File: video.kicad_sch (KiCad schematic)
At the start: 53 parts, among them IC103 HUC6260, IC108 UPC358, J1 RF, Q101 25C945, Q102 25A733, Q103 25C945

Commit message: Work out numbering of and route some caps.
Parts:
- C101: footprint (none) -> A-PCENGINE:Elec_P5.00mm
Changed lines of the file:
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@@
       (effects (font (size 1.27 1.27)))
     )
-    (property "Footprint" "" (at 102.87 93.6752 0)
+    (property "Footprint" "A-PCENGINE:Elec_P5.00mm" (at 102.87 93.6752 0)
       (effects (font (size 1.27 1.27)) hide)
     )
@@
         )
         (path "/c1c718c6-a427-431e-a18b-e46f94ae8e09/c78d7e8a-3e65-46f4-91f4-96eb31925bea"
-          (reference "C141") (unit 1)
+          (reference "C108") (unit 1)
         )
       )
@@
         )
         (path "/c1c718c6-a427-431e-a18b-e46f94ae8e09/c78d7e8a-3e65-46f4-91f4-96eb31925bea"
-          (reference "C112") (unit 1)
+          (reference "CX112") (unit 1)
         )
       )
@@
       (effects (font (size 1.27 1.27)))
     )
-    (property "Footprint" "" (at 102.87 127.9652 0)
+    (property "Footprint" "A-PCENGINE:Elec_P5.00mm" (at 102.87 127.9652 0)
       (effects (font (size 1.27 1.27)) hide)
     )
@@
         )
         (path "/c1c718c6-a427-431e-a18b-e46f94ae8e09/c78d7e8a-3e65-46f4-91f4-96eb31925bea"
-          (reference "C146") (unit 1)
+          (reference "C114") (unit 1)
         )
       )
@@
       (effects (font (size 1.27 1.27)))
     )
-    (property "Footprint" "" (at 91.44 110.1852 0)
+    (property "Footprint" "A-PCENGINE:Elec_P5.00mm" (at 91.44 110.1852 0)
       (effects (font (size 1.27 1.27)) hide)
     )
@@
         )
         (path "/c1c718c6-a427-431e-a18b-e46f94ae8e09/c78d7e8a-3e65-46f4-91f4-96eb31925bea"
-          (reference "C144") (unit 1)
+          (reference "C111") (unit 1)
         )
       )
@@
       (effects (font (size 1.27 1.27)))
     )
-    (property "Footprint" "" (at 91.44 133.0452 0)
+    (property "Footprint" "A-PCENGINE:Elec_P5.00mm" (at 91.44 133.0452 0)
       (effects (font (size 1.27 1.27)) hide)
     )
@@
         )
         (path "/c1c718c6-a427-431e-a18b-e46f94ae8e09/c78d7e8a-3e65-46f4-91f4-96eb31925bea"
-          (reference "C149") (unit 1)
+          (reference "C115") (unit 1)
         )
       )
@@
       (effects (font (size 1.27 1.27)))
     )
-    (property "Footprint" "" (at 102.87 105.1052 0)
+    (property "Footprint" "A-PCENGINE:Elec_P5.00mm" (at 102.87 105.1052 0)
       (effects (font (size 1.27 1.27)) hide)
     )
@@
         )
         (path "/c1c718c6-a427-431e-a18b-e46f94ae8e09/c78d7e8a-3e65-46f4-91f4-96eb31925bea"
-          (reference "C145") (unit 1)
+          (reference "C110") (unit 1)
         )
       )
@@
         )
         (path "/c1c718c6-a427-431e-a18b-e46f94ae8e09/c78d7e8a-3e65-46f4-91f4-96eb31925bea"
-          (reference "C114") (unit 1)
+          (reference "CX114") (unit 1)
         )
       )
@@
       (effects (font (size 1.27 1.27)))
     )
-    (property "Footprint" "" (at 102.87 139.3952 0)
+    (property "Footprint" "A-PCENGINE:Elec_P5.00mm" (at 102.87 139.3952 0)
       (effects (font (size 1.27 1.27)) hide)
     )
@@
         )
         (path "/c1c718c6-a427-431e-a18b-e46f94ae8e09/c78d7e8a-3e65-46f4-91f4-96eb31925bea"
-          (reference "C142") (unit 1)
+          (reference "C116") (unit 1)
         )
       )
@@
       (effects (font (size 1.27 1.27)))
     )
-    (property "Footprint" "" (at 102.87 116.5352 0)
+    (property "Footprint" "A-PCENGINE:Elec_P5.00mm" (at 102.87 116.5352 0)
       (effects (font (size 1.27 1.27)) hide)
     )
@@
         )
         (path "/c1c718c6-a427-431e-a18b-e46f94ae8e09/c78d7e8a-3e65-46f4-91f4-96eb31925bea"
-          (reference "C148") (unit 1)
+          (reference "C112") (unit 1)
         )
       )
@@
       (effects (font (size 1.27 1.27)))
     )
-    (property "Footprint" "" (at 91.44 121.6152 0)
+    (property "Footprint" "A-PCENGINE:Elec_P5.00mm" (at 91.44 121.6152 0)
       (effects (font (size 1.27 1.27)) hide)
     )
@@
         )
         (path "/c1c718c6-a427-431e-a18b-e46f94ae8e09/c78d7e8a-3e65-46f4-91f4-96eb31925bea"
-          (reference "C147") (unit 1)
+          (reference "C113") (unit 1)
         )
       )
@@
       (effects (font (size 1.27 1.27)))
     )
-    (property "Footprint" "" (at 351.4852 101.6 0)
+    (property "Footprint" "A-PCENGINE:Elec_P5.00mm" (at 351.4852 101.6 0)
       (effects (font (size 1.27 1.27)) hide)
     )
@@
       (effects (font (size 1.27 1.27)))
     )
-    (property "Footprint" "" (at 91.44 98.7552 0)
+    (property "Footprint" "A-PCENGINE:Elec_P5.00mm" (at 91.44 98.7552 0)
       (effects (font (size 1.27 1.27)) hide)
     )
@@
         )
         (path "/c1c718c6-a427-431e-a18b-e46f94ae8e09/c78d7e8a-3e65-46f4-91f4-96eb31925bea"
-          (reference "C143") (unit 1)
-        )
-      )
+          (reference "C109") (unit 1)
+        )
+      )

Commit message: Intermediate save
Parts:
- C104, C105, C106, C107: footprint (none) -> A-PCENGINE:SMD_1206_C
- C107, R103, R104: footprint (none) -> A-PCENGINE:SMD_1206
- FL103: footprint (none) -> A-PCENGINE:FL-5.00mm
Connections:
- net +5V: now also IC103.1 (VCC), IC103.13 (VCC), IC103.16 (VCC), IC103.53 (VCC), IC103.54 (VCC), IC103.57 (VCC)
- net +5VA: now also IC103.21 (AVCC), IC103.27 (AVCC), IC103.34 (AVCC), IC103.36 (AVCC), IC103.41 (AVCC), IC103.50 (AVCC)
- net GND: now also IC103.14 (GND), IC103.15 (GND), IC103.3 (GND), IC103.55 (GND), IC103.56 (GND); no longer R103.2
- net GNDA: now also IC103.19 (AGND), IC103.25 (AGND), IC103.29 (AGND), IC103.32 (AGND), IC103.39 (AGND), IC103.48 (AGND)
- new net OSC_GND: R103.2
- no-connect marks 1 -> 4

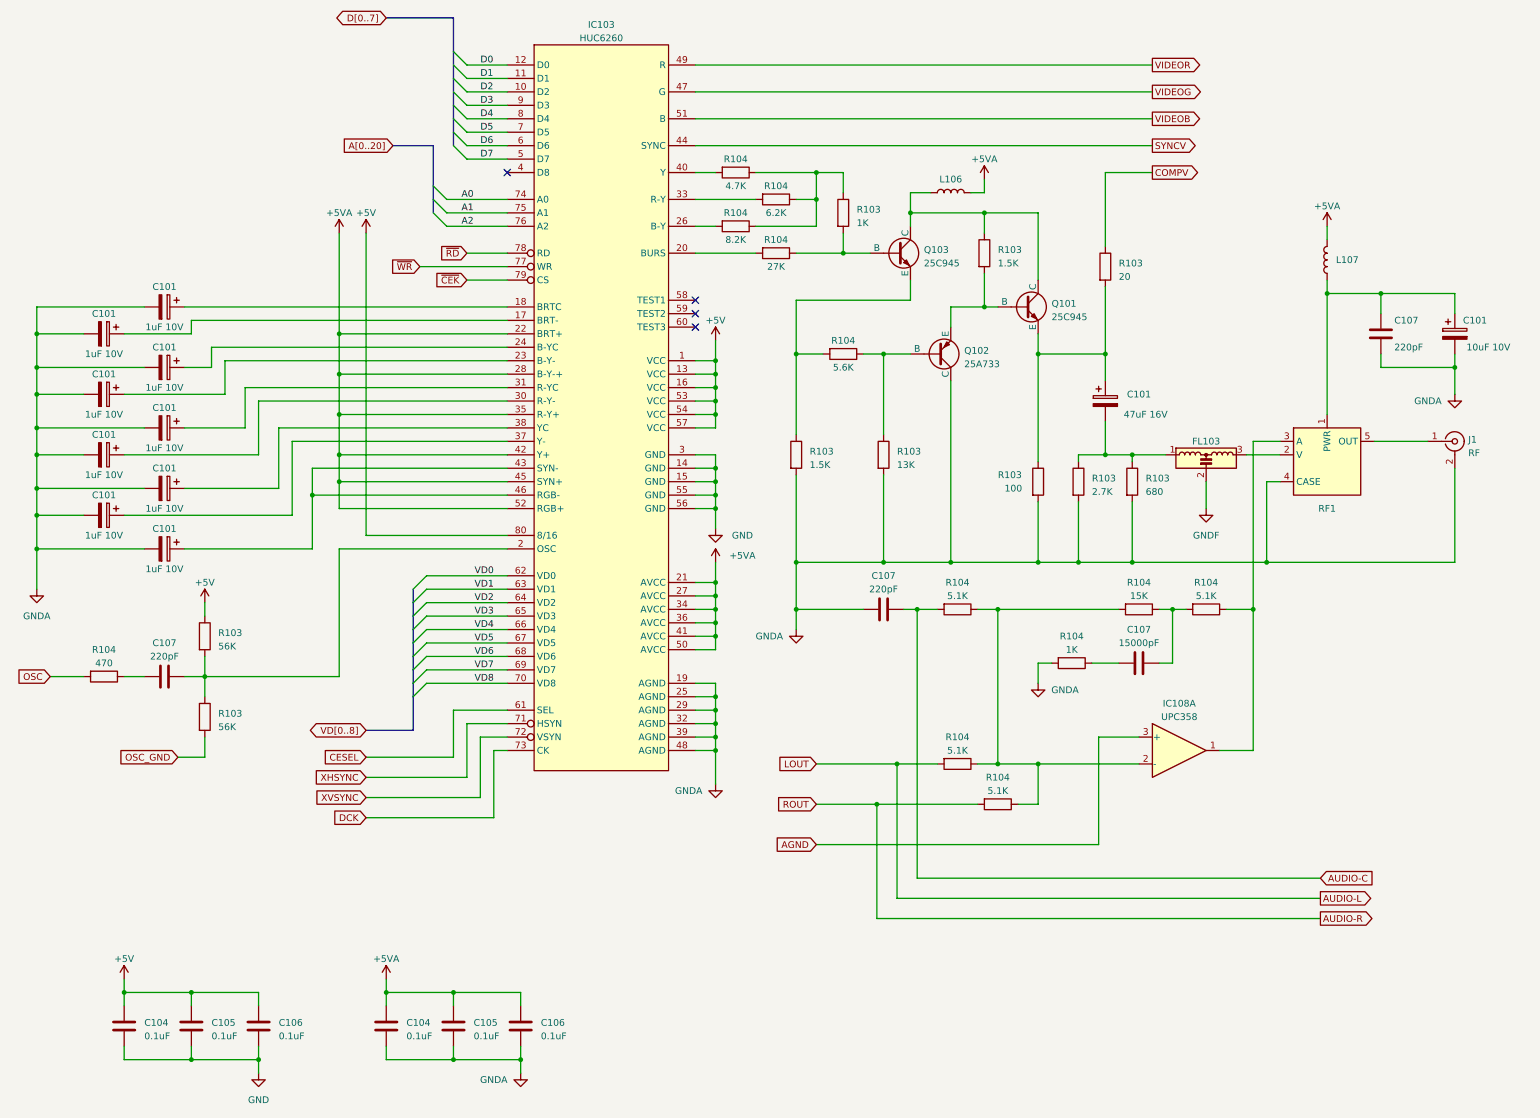
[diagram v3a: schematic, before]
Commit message: Finish basic routing, resolve DRC errors.
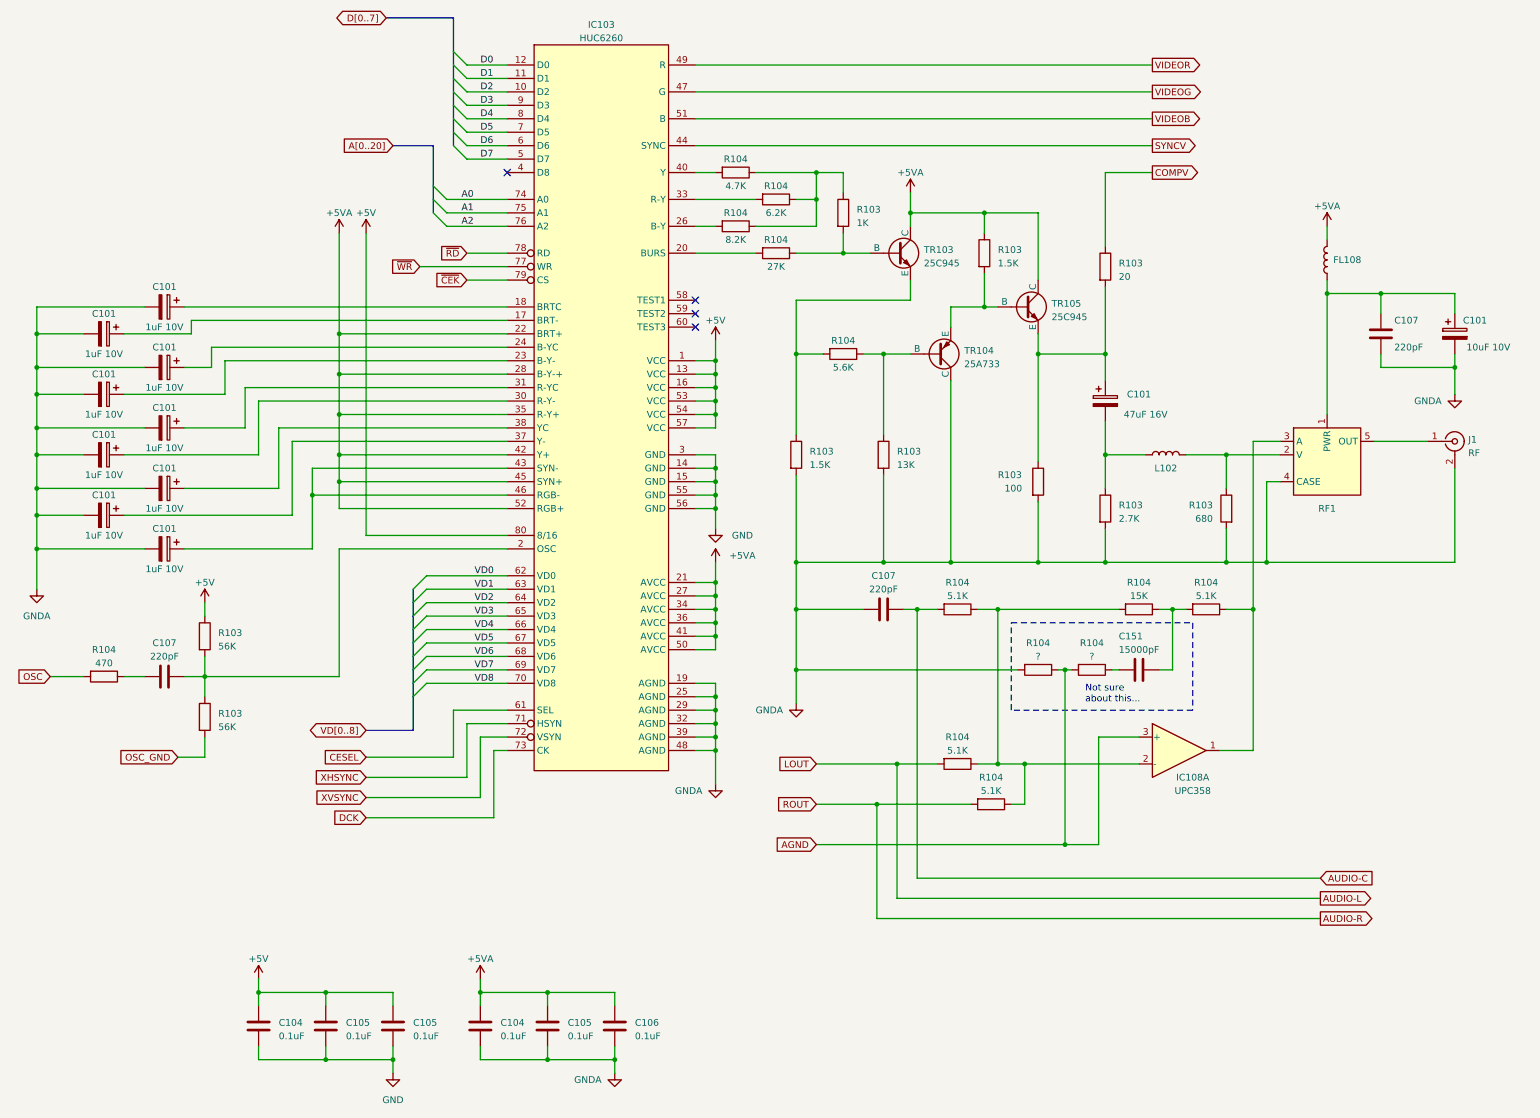
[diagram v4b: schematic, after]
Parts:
- removed C106: 0.1uF, A-PCENGINE:SMD_1206_C, symbol Device:C
- removed C107: 15000pF, A-PCENGINE:SMD_1206_C, symbol Device:C
- removed FL103: Filter_EMI_LCL, A-PCENGINE:FL-5.00mm, symbol Device:Filter_EMI_LCL
- removed L106: ~, symbol Device:L
- removed R104: 1K, symbol Device:R
- added C105: 0.1uF, A-PCENGINE:SMD_1206_C, symbol Device:C
- added C151: 15000pF, A-PCENGINE:SMD_1206_C, symbol Device:C
- added L102: ~, A-PCENGINE:L-5.00mm, symbol Device:L
- added R104 (x2): ?, A-PCENGINE:SMD_1206, symbol Device:R
- C101: footprint (none) -> A-PCENGINE:Elec_P5.00mm
- C107: footprint A-PCENGINE:SMD_1206_C -> A-PCENGINE:SMD_1206
- FL108: renamed from L107; footprint (none) -> A-PCENGINE:L-5.00mm
- IC108: footprint (none) -> Package_DIP:DIP-8_W7.62mm_LongPads
- R103, R104: footprint (none) -> A-PCENGINE:SMD_1206
- RF1: footprint (none) -> A-PCENGINE:CN103
- TR103: renamed from Q103; footprint (none) -> A-PCENGINE:Transistor_SMD
- TR104: renamed from Q102; footprint (none) -> A-PCENGINE:Transistor_SMD
- TR105: renamed from Q101; footprint (none) -> A-PCENGINE:Transistor_SMD
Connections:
- net +5V: now also C105.1
- net +5VA: now also R103.1, TR103.1 (C), TR105.1 (C)
- net AGND: now also R104.1, R104.2
- net GND: now also C105.2
- net GNDA: now also R104.2
- net at RF1.2 (V): now also R103.1, L102.2
- net at R104.1, R104.2: now also C151.1
- net at C101.2, R103.1: now also L102.1; no longer R103.1
- new net: C151.2, R104.1
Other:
- note added: "Not sure about this..."
- moved on the sheet: C104, C105, C106, R103, R104

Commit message: First draft of complete PCB.
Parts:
- removed FL108: ~, A-PCENGINE:L-5.00mm, symbol Device:L
- removed J1: RF, symbol Connector:Conn_Coaxial
- added FL101: Filter_EMI_LCL, A-PCENGINE:FL-5.00mm, symbol Device:Filter_EMI_LCL
- IC108: value UPC358 -> μPC358C; footprint Package_DIP:DIP-8_W7.62mm_LongPads -> A-PCENGINE:DIP-8
- R103: value 680 -> 6.8K
- R104: value ? -> 10K
- R104: value 5.6K -> 3.3K
- R104: value 5.1K -> 4.1K
- R104: value 470 -> 1.2K
- renumbered RF1 to CN103
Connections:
- net OSC_GND is gone; now on net GND: R103.2
- net +5VA: now also FL101.3
- net GNDA: now also FL101.2
- net at C101.1, C107.2, CN103.1 (PWR): now also FL101.1
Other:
- note removed: "Not sure about this..."
- moved on the sheet: C101, C107, R104

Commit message: Verify passive values.
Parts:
- C101: value 1uF 10V -> 10uF 16V
- C107: value 220pF -> 0.1uF L
- R104: value 4.1K -> 9.1K
- R104: value 10K -> 1K
- R104: value 8.2K -> 8.1K
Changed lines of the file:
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@@
       (effects (font (size 1.27 1.27)))
     )
-    (property "Value" "4.1K" (at 252.73 176.53 90)
+    (property "Value" "9.1K" (at 252.73 176.53 90)
       (effects (font (size 1.27 1.27)))
     )
@@
       (effects (font (size 1.27 1.27)) (justify right))
     )
-    (property "Value" "220pF" (at 341.63 100.33 0)
+    (property "Value" "0.1uF L" (at 341.63 100.33 0)
       (effects (font (size 1.27 1.27)) (justify right))
     )
@@
       (effects (font (size 1.27 1.27)))
     )
-    (property "Value" "10K" (at 280.67 158.75 90)
+    (property "Value" "1K" (at 280.67 158.75 90)
       (effects (font (size 1.27 1.27)))
     )
@@
       (effects (font (size 1.27 1.27)))
     )
-    (property "Value" "4.1K" (at 252.73 147.32 90)
+    (property "Value" "9.1K" (at 252.73 147.32 90)
       (effects (font (size 1.27 1.27)))
     )
@@
       (effects (font (size 1.27 1.27)))
     )
-    (property "Value" "1uF 10V" (at 106.68 142.24 90)
+    (property "Value" "10uF 16V" (at 106.68 142.24 90)
       (effects (font (size 1.27 1.27)))
     )
@@
       (effects (font (size 1.27 1.27)))
     )
-    (property "Value" "8.2K" (at 214.63 80.01 90)
+    (property "Value" "8.1K" (at 214.63 80.01 90)
       (effects (font (size 1.27 1.27)))
     )
@@
       (effects (font (size 1.27 1.27)))
     )
-    (property "Value" "4.1K" (at 260.35 184.15 90)
-      (effects (font (size 1.27 1.27)))
-    )
+    (property "Value" "9.1K" (at 260.35 184.15 90)
+      (effects (font (size 1.27 1.27)))
+    )
